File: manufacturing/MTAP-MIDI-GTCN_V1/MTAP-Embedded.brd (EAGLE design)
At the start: 30.5 x 45.1 mm, 34 parts, among them IC1 ESP32-WROOM-32UE-N8, IC2 AMS1117-3.3, J1 629105150521

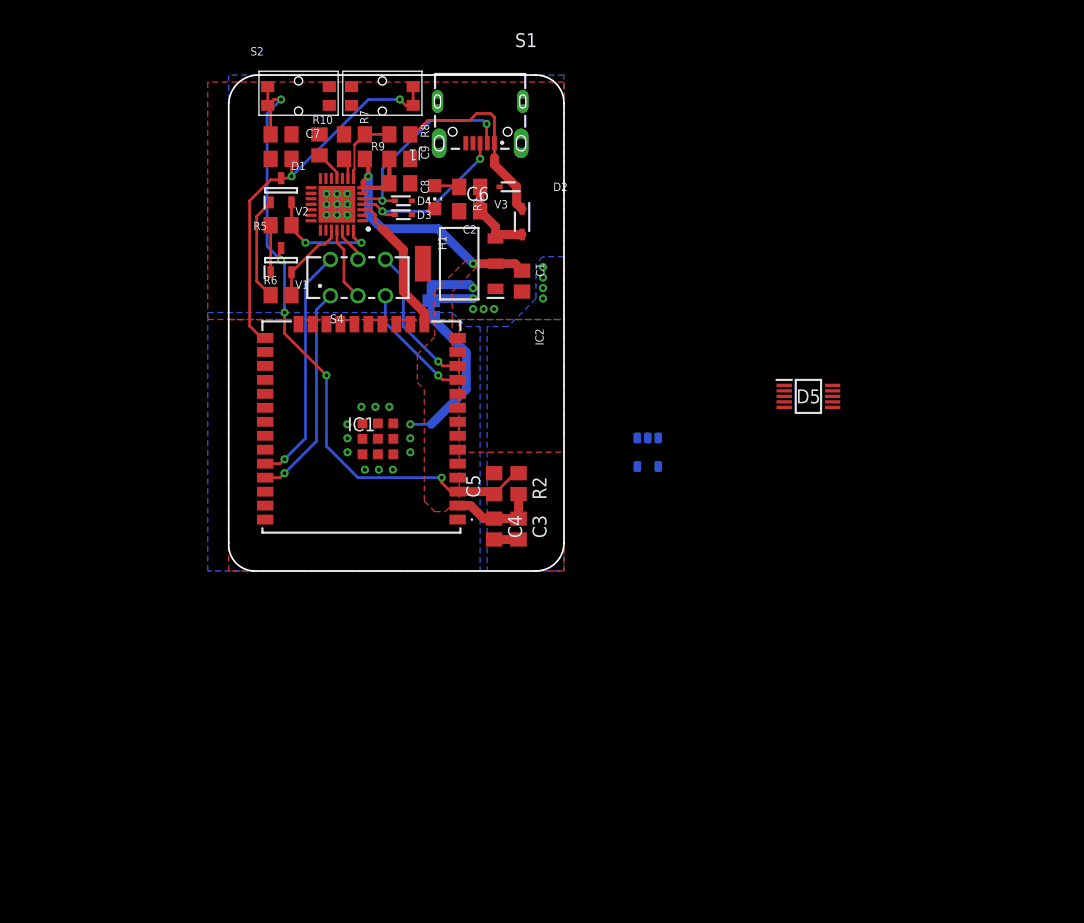
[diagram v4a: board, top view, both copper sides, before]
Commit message: upd pcb analog
new filter
new ADC
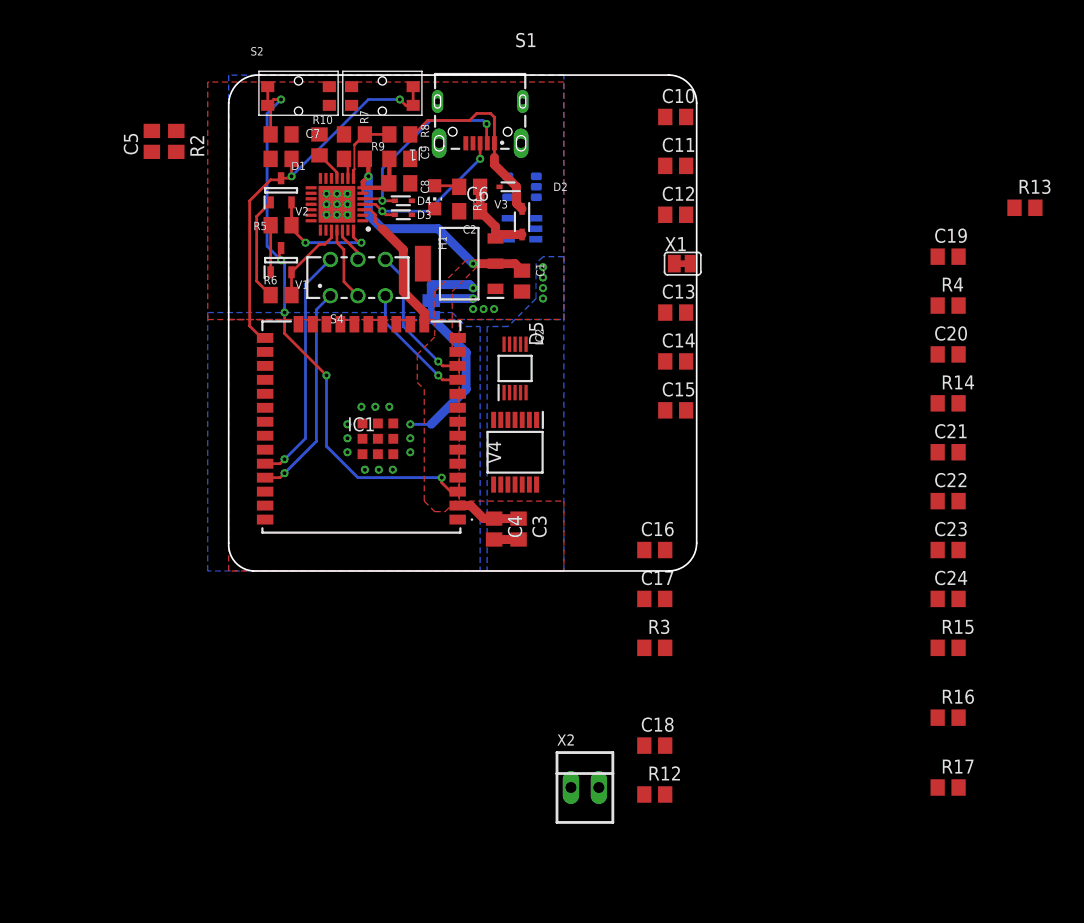
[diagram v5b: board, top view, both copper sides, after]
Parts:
- added C10, C11, C12, C14, C15: 1u, rcl_GruS:C0805
- added C13: 10n, rcl_GruS:C0805
- added C16, C17, C18, C19, C20, C21, C22, C23, C24: (no value), rcl_GruS:C0805
- added IC3: TPS60402DBVT, vreg_GruS:SOT95P280X145-5N
- added R12, R13, R14, R3: (no value), rcl_GruS:R0805
- added R15, R16, R17, R4: 33R, rcl_GruS:R0805
- added V4: TLV9104IPWR, opv_GruS:SOP65P640X120-14N
- added X1: (no value), con_GruS:MYLIB_SJ-SHORT
- added X2: 22-23-2021, con-molex:22-23-2021
- moved C5 44.0 mm to (-12.1, 54.3)
- moved R2 44.0 mm to (-9.84, 54.3)
- moved D5 26.8 mm to (21.0, 33.7), turned to 90 degrees
- moved N1 26.7 mm to (21.6, 50.2), turned to 0 degrees
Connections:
- net N$11 renamed AINP
- removed net ADI: D5.9
- new net !CS: R17.2
- new net -1V8: C12.1, IC3.1, V4.11
- new net AINN: D5.4
- new net MISO: R16.2
- new net MOSI: R4.2
- new net N$11: D5.7, R16.1
- new net N$12: C18.1, R13.2, V4.5
- new net N$13: C17.1, V4.6, V4.7
- new net N$14: D5.8, R15.1
- new net N$17: C10.2, IC3.3
- new net N$18: C10.1, IC3.5
- new net N$19: D5.9, R4.1
- new net N$5: D5.6, R17.1
- new net SCLK: R15.2
- new net VREF: C20.1, C21.1, D5.1, X1.2
- net +1V8: now also C11.1, C14.1, C22.1, C23.1, IC3.2, V4.4
- net +3V3: now also C15.1, C24.1, D5.10, N1.3
- net +5V: now also X1.1
- net AGND: now also C16.2, C18.2, C20.2, C21.2, C22.2, C23.2, C24.2, X2.1; no longer D5.4, N1.4
- net N$10: now also C13.1
- net N$6: now also R12.1, V4.1, V4.2; no longer D5.7
- net N$7: now also C16.1, R3.2, V4.3; no longer D5.8
- net N$8: now also R3.1, X2.2; no longer N1.3
- net N$9: now also C17.2, R12.2, R13.1; no longer D5.1
- net PGND: now also C11.2, C12.2, C13.2, C14.2, C15.2, IC3.4, N1.4
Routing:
- net EN: track 61.7 -> 55.9 mm
- net +3V3: track 36.1 -> 33.9 mm
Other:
- board size 30.5 x 45.1 mm -> 42.5 x 45.1 mm

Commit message: upd analog
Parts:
- removed C19: (no value), rcl_GruS:C0805
- removed R14: (no value), rcl_GruS:R0805
- C16: value (none) -> 10n
- C17: value (none) -> 180n
- C18: value (none) -> 10nF
- C20, C22: value (none) -> 100n
- C21, C23: value (none) -> 1u
- R12: value (none) -> 560R
- R13: value (none) -> 1k
- R3: value (none) -> 6k2
- moved N1 0.63 mm to (21.6, 49.5)
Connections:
- removed net N$13: C17.1, V4.6, V4.7
- net AINP: now also C17.1, V4.6, V4.7

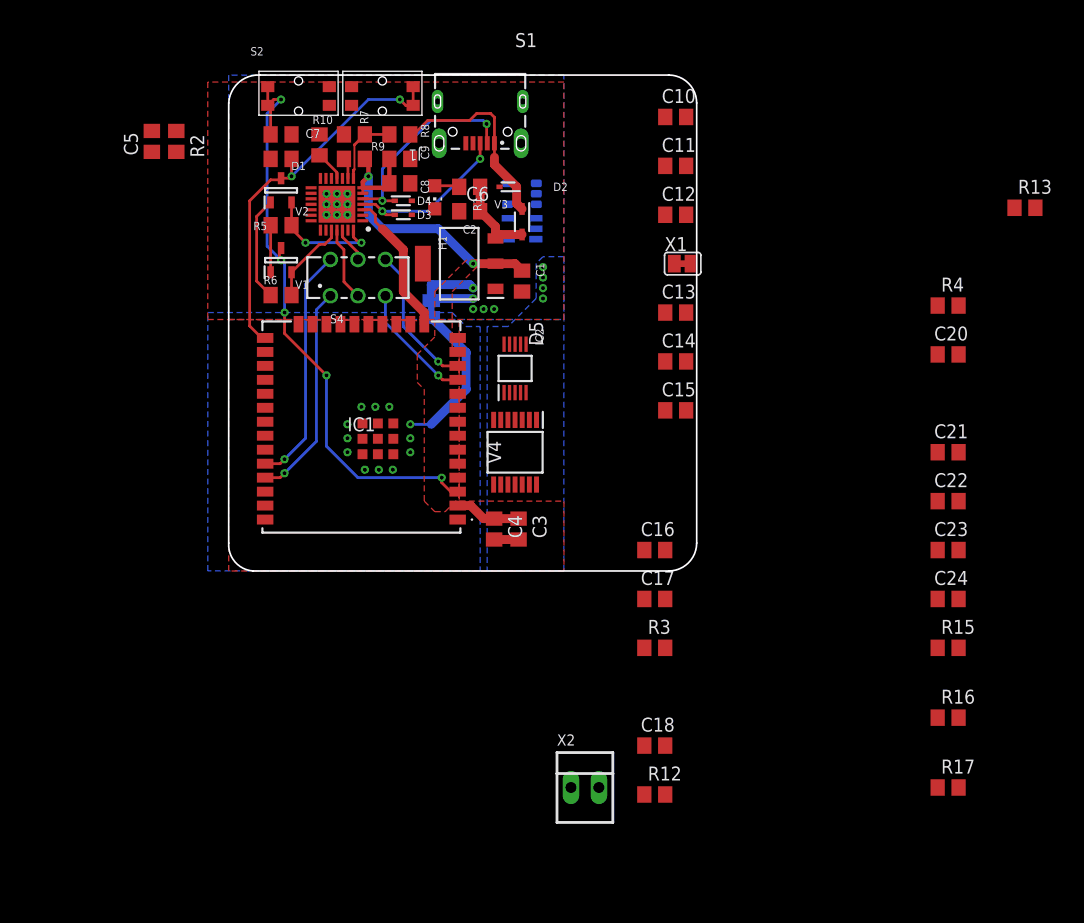
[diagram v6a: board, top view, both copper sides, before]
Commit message: upd schematic to fix adc problem
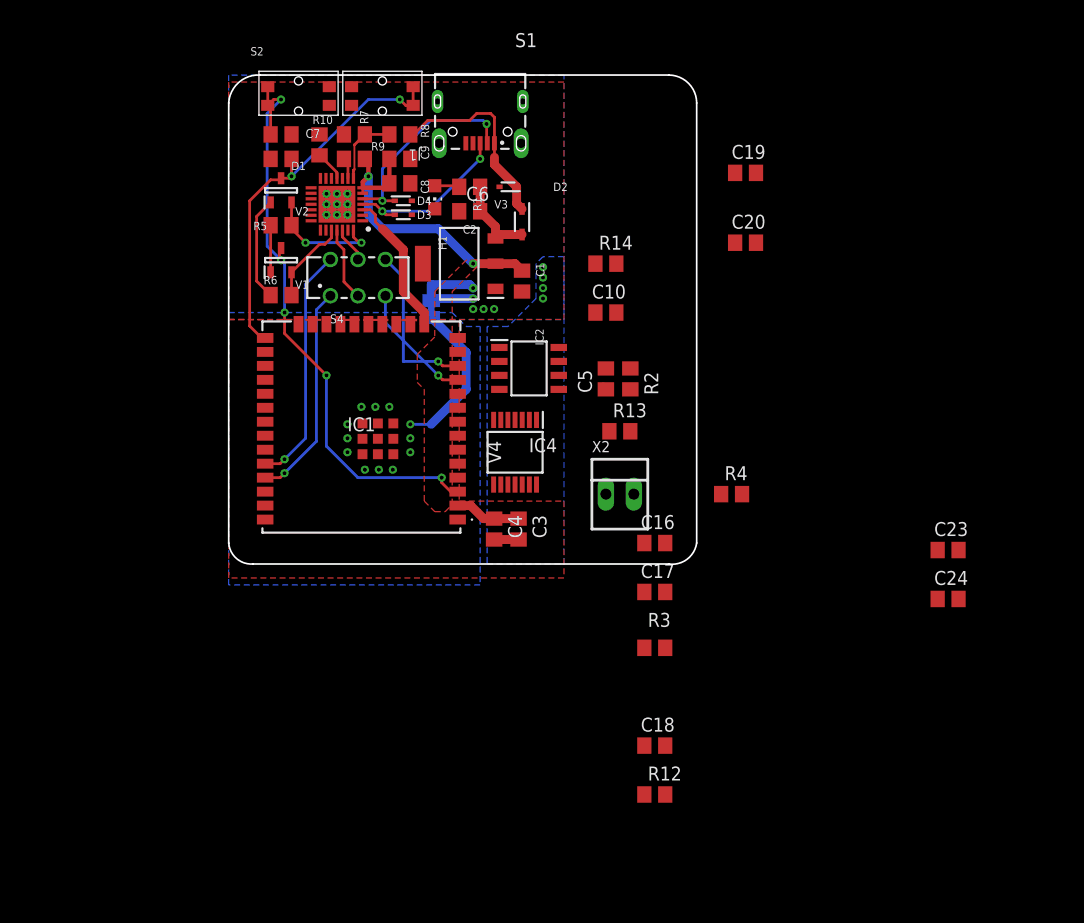
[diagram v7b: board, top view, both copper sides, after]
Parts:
- removed C11, C12, C14, C15, C21: 1u, rcl_GruS:C0805
- removed C13: 10n, rcl_GruS:C0805
- removed C22: 100n, rcl_GruS:C0805
- removed D5: MCP33131-05-E, adc-dac_GruS:MSOP10
- removed IC3: TPS60402DBVT, vreg_GruS:SOT95P280X145-5N
- removed N1: TC2015, vreg_GruS:SOT-23-5
- removed R15, R16, R17: 33R, rcl_GruS:R0805
- removed X1: (no value), con_GruS:MYLIB_SJ-SHORT
- added C19: 1u, rcl_GruS:C0805
- added IC4: MCP3001T-I_SN, adc-dac_GruS:SOIC127P600X175-8N
- added R14: (no value), rcl_GruS:R0805
- C10: value 1u -> (none)
- C24: value (none) -> 1u
- R4: value 33R -> (none)
- moved C5 46.6 mm to (29.2, 32.7)
- moved R2 46.6 mm to (31.4, 32.7)
- moved R13 42.1 mm to (30.5, 27.9)
- moved X2 26.9 mm to (30.5, 22.2)
- moved R4 26.1 mm to (40.6, 22.2)
- moved C20 21.0 mm to (41.9, 45.1)
- moved C10 18.9 mm to (29.2, 38.7)
- moved C16 0.64 mm to (33.7, 17.8)
- moved C17 0.64 mm to (33.7, 13.3)
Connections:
- removed net +1V8: C11.1, C14.1, C22.1, C23.1, D5.2, IC3.2, N1.5, V4.4
- removed net -1V8: C12.1, IC3.1, V4.11
- removed net AINN: D5.4
- removed net MOSI: R4.2
- removed net N$10: C13.1, N1.2
- removed net N$11: D5.7, R16.1
- removed net N$14: D5.8, R15.1
- removed net N$18: C10.1, IC3.5
- removed net N$19: D5.9, R4.1
- removed net N$5: D5.6, R17.1
- removed net VREF: C20.1, C21.1, D5.1, X1.2
- net !CS: now also IC4.5; no longer R17.2
- net +3V3: now also C20.1, C23.1, IC4.1, IC4.8, R4.2, V4.4; no longer C15.1, D5.10, N1.1, N1.3
- net +5V: no longer X1.1
- net AGND: now also C19.2, IC4.3, IC4.4, R14.1, V4.11; no longer C21.2, C22.2, D5.5
- net AINP: now also C19.1, IC4.2; no longer D5.3
- net MISO: now also IC4.6; no longer R16.2
- net N$17: now also R14.2, R4.1, X2.2; no longer IC3.3
- net N$8: now also C10.1; no longer X2.2
- net PGND: no longer C11.2, C12.2, C13.2, C14.2, C15.2, IC3.4, N1.4
- net SCLK: now also IC4.7; no longer R15.2
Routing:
- net RXD1: track 13.2 -> 15.1 mm
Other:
- board size 42.5 x 45.1 mm -> 42.5 x 44.5 mm

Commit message: update analogue process chain onboard
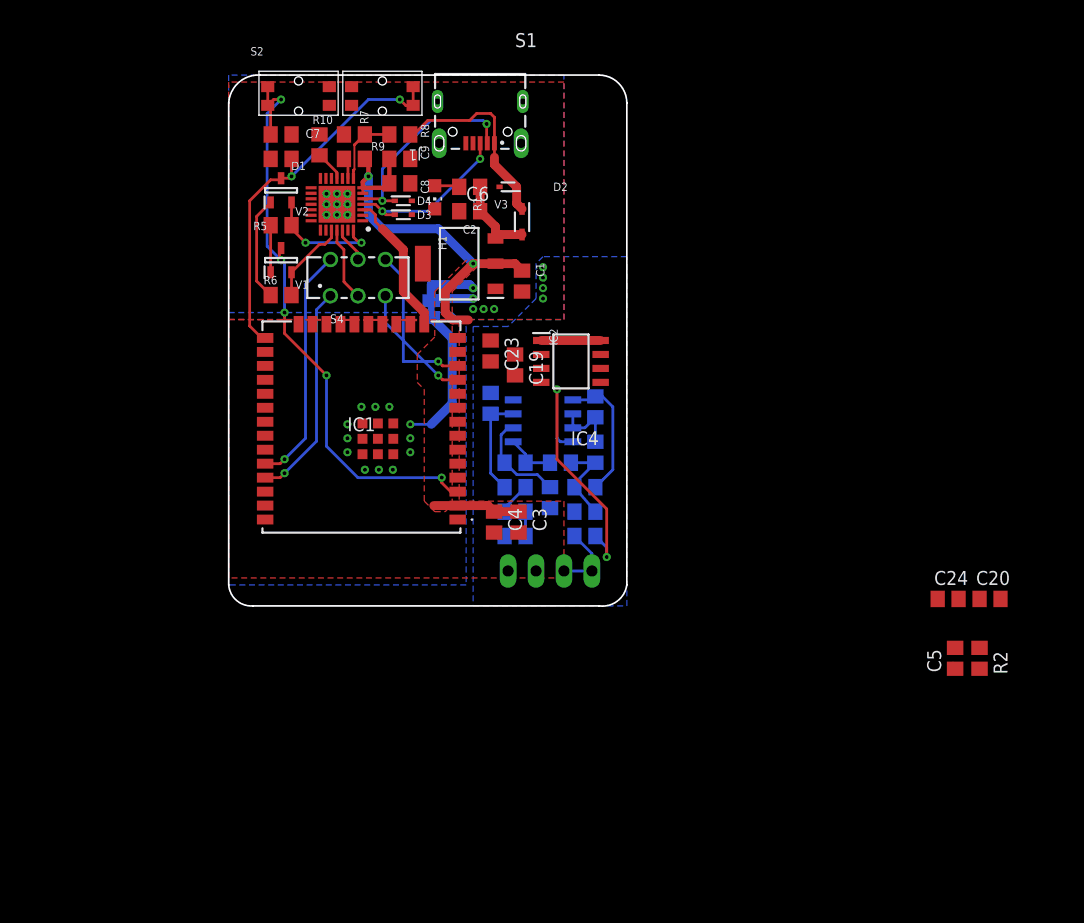
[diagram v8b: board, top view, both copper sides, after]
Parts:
- removed C17: 180n, rcl_GruS:C0805
- removed V4: TLV9104IPWR, opv_GruS:SOP65P640X120-14N
- removed X2: 22-23-2021, con-molex:22-23-2021
- added C11: 100n, rcl_GruS:C0805
- added R15: 560R, rcl_GruS:R0805
- added R16: 10k, rcl_GruS:R0805
- added R34: 180n, rcl_GruS:R0805
- added V5: TLV9152QDRQ1, opv_GruS:SOIC127P600X175-8N
- added X1: (no value), con-lstb:MA04-1
- C10: value (none) -> 100n
- R14, R4: value (none) -> 10k
- moved C23 45.4 mm to (18.7, 35.2), turned to 270 degrees
- moved C5 40.7 mm to (61.0, 7.30)
- moved R2 40.7 mm to (63.2, 7.30)
- moved C20 39.3 mm to (64.1, 12.7)
- moved R12 31.4 mm to (25.1, 25.1), flipped to the bottom, turned to 180 degrees
- moved C19 27.3 mm to (21.0, 34.0), turned to 270 degrees
- moved R14 26.1 mm to (21.0, 18.4), flipped to the bottom, turned to 180 degrees
- moved C18 22.2 mm to (27.3, 20.6), flipped to the bottom
- moved C10 19.9 mm to (21.0, 20.6), flipped to the bottom, turned to 180 degrees
- moved C16 19.6 mm to (18.7, 30.5), flipped to the bottom, turned to 90 degrees
- moved R3 19.4 mm to (21.0, 22.9), flipped to the bottom
- moved R4 13.9 mm to (27.3, 18.4), flipped to the bottom, turned to 180 degrees
- moved R13 5.99 mm to (27.3, 22.9), flipped to the bottom, turned to 180 degrees
- moved IC4 3.86 mm to (26.0, 34.3)
- moved C3 0.63 mm to (21.3, 19.7)
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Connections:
- new net N$5: R15.1, R16.2, V5.2
- net +3V3: now also V5.8; no longer V4.4
- net AGND: now also R16.1, V5.4, X1.1, X1.2; no longer V4.11, X2.1
- net AINP: now also C11.1, R34.1, V5.6, V5.7; no longer C17.1, V4.6, V4.7
- net N$12: now also C11.2, V5.5; no longer C18.1, V4.5
- net N$17: now also X1.3, X1.4; no longer X2.2
- net N$6: now also R15.2, V5.1; no longer V4.1, V4.2
- net N$7: now also V5.3; no longer V4.3
- net N$9: now also C18.1, R34.2; no longer C17.2
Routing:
- net +3V3: track 33.9 -> 74.5 mm, vias 2 -> 4
- net N$12: track 0.00 -> 12.1 mm
- net N$7: track 0.00 -> 9.25 mm
- net N$5: track 0.00 -> 9.08 mm
- net N$17: track 0.00 -> 8.91 mm
- net N$9: track 0.00 -> 8.80 mm
- net AINP: track 0.00 -> 6.41 mm
- net N$6: track 0.00 -> 4.80 mm
- net GND: track 29.8 -> 26.3 mm
- net N$8: track 0.00 -> 3.01 mm
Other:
- board size 42.5 x 44.5 mm -> 36.2 x 48.3 mm
